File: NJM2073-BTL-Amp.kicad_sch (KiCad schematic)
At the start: 84 parts, among them J1 Screw_Terminal_01x02, J2 Screw_Terminal_01x02, J3 Barrel_Jack_Switch, J4 Conn_Coaxial_x2, J5 AudioJack3_SwitchTR, U1 NJM2073, U2 NJM2073, U3 NJM4558, U4 NJM4558, U5 LM317_TO-220

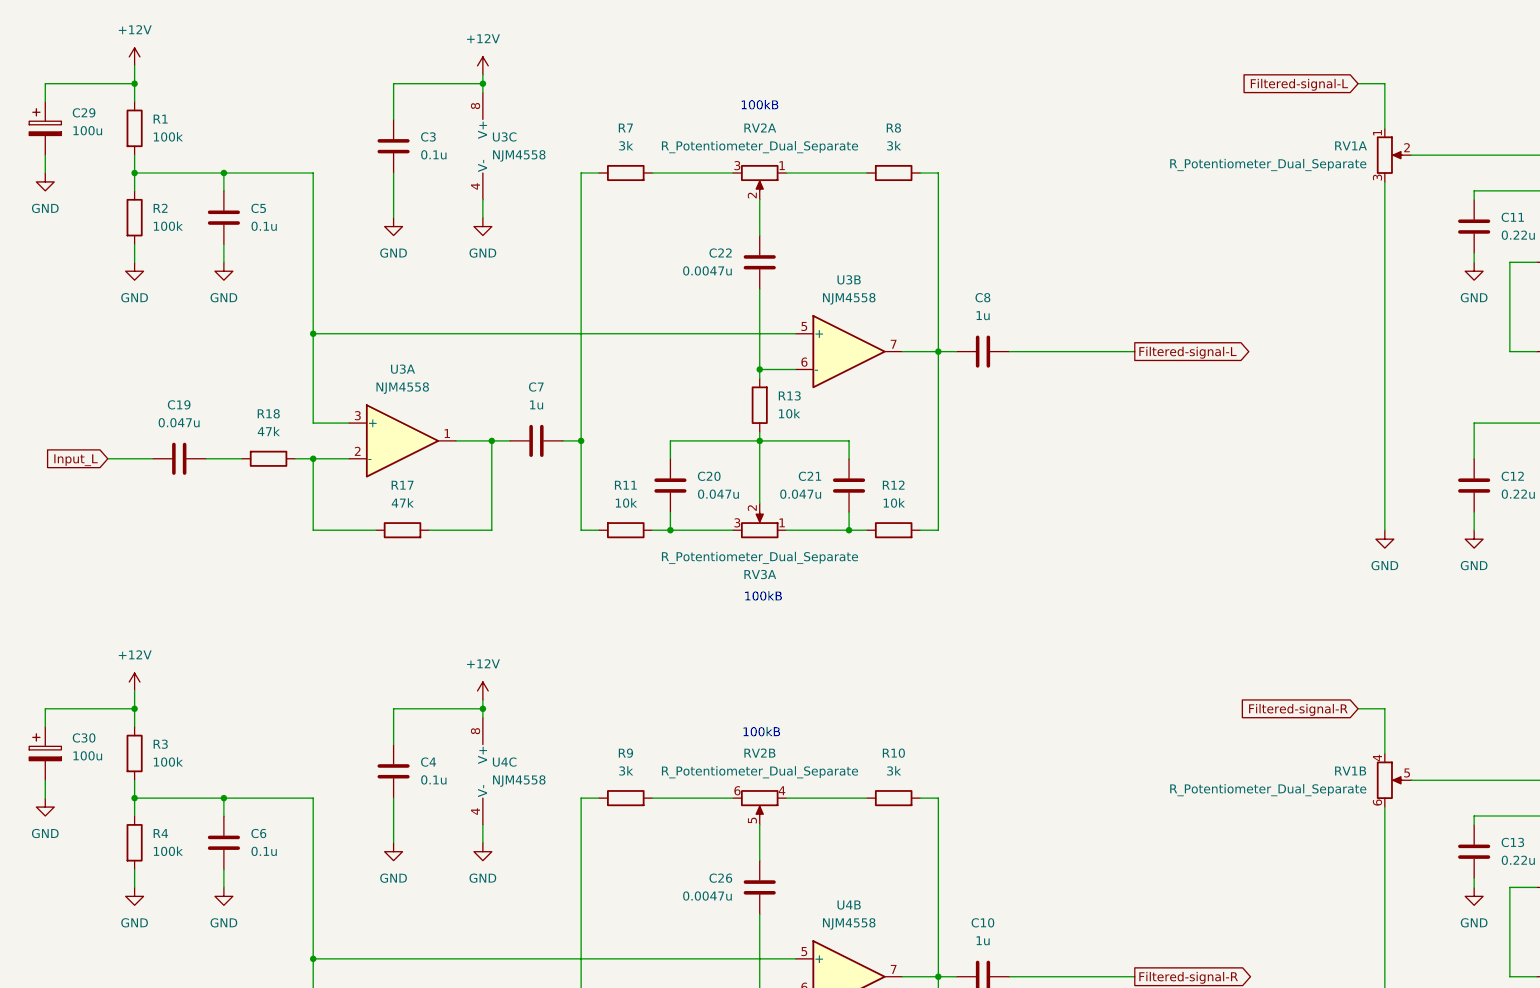
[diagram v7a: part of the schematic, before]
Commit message: 配線修正
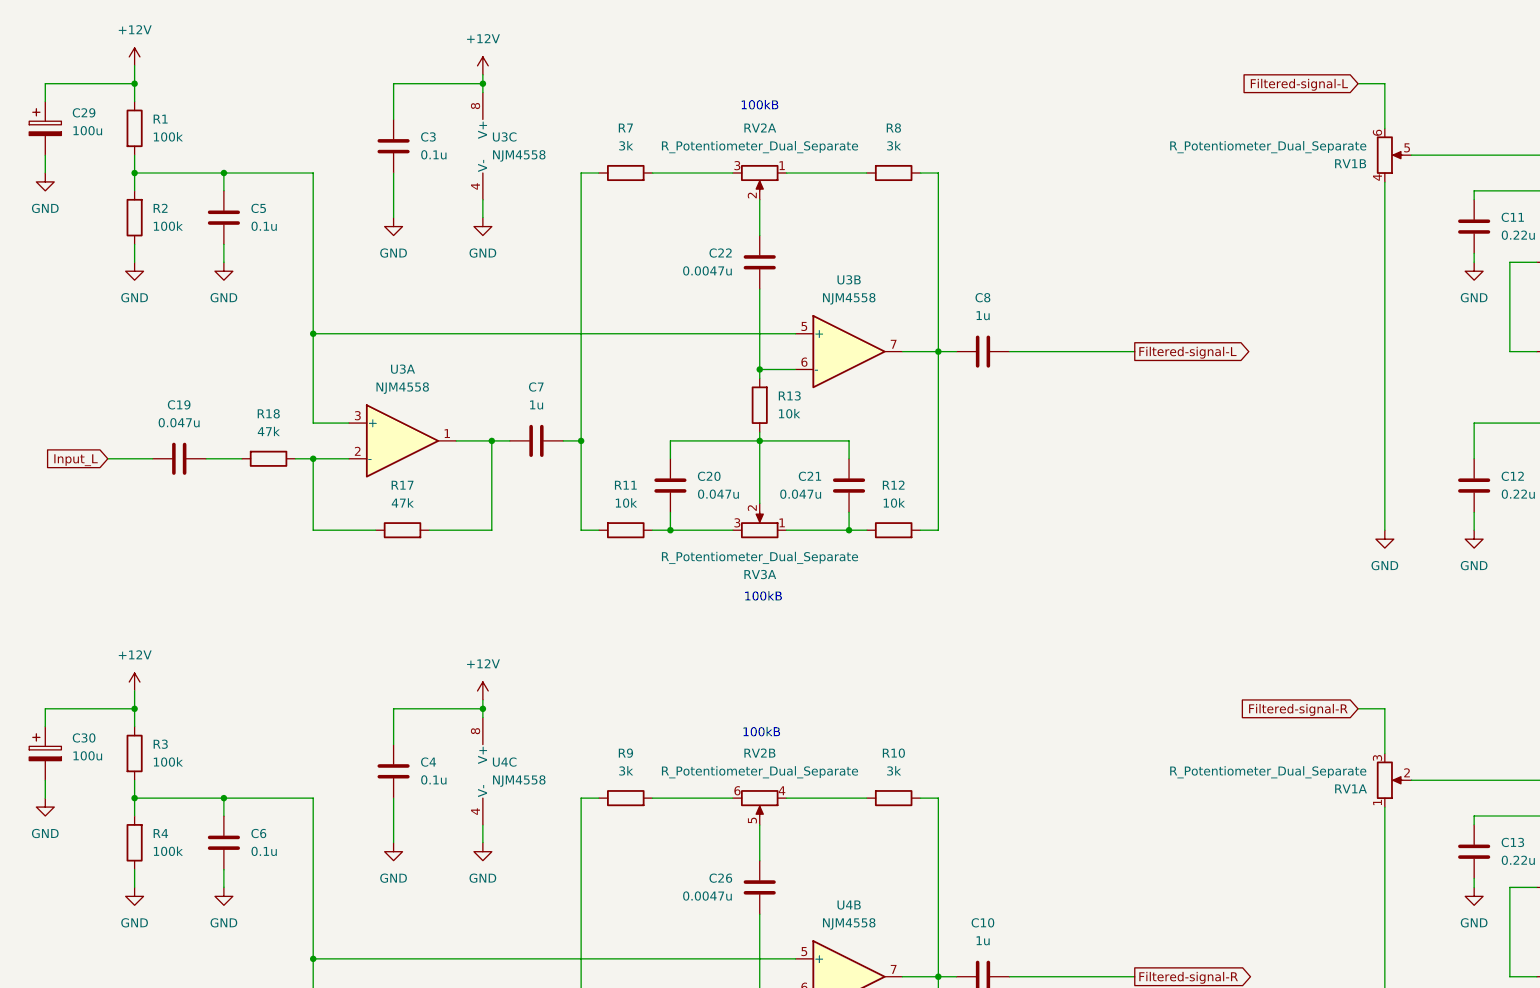
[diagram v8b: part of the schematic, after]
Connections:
- net Filtered-signal-L: now also RV1.6; no longer RV1.1
- net Filtered-signal-R: now also RV1.3; no longer RV1.4
- net GND: now also R2.1, R4.1, RV1.1, RV1.4; no longer R2.2, R4.2, RV1.3, RV1.6
- net at U2.7 (AIN+): now also RV1.2; no longer RV1.5
- net at C6.1, R3.2, U4.3 (+)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: now also R4.2; no longer R4.1
- net at C10.1, R15.2, U4.7: now also R10.1; no longer R10.2
- net at C5.1, R1.2, U3.3 (+)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: now also R2.2; no longer R2.1
- net at U1.7 (AIN+): now also RV1.5; no longer RV1.2
- net at RV2.4: now also R10.2; no longer R10.1
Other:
- moved on the sheet: R10, R2, R4
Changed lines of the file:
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@@
 	)
 	(symbol
+		(lib_id "Device:R_Potentiometer_Dual_Separate")
+		(at 292.1 137.16 0)
+		(mirror x)
+		(unit 1)
+		(exclude_from_sim no)
+		(in_bom yes)
+		(on_board yes)
+		(dnp no)
+		(property "Reference" "RV1"
+			(at 289.56 138.4301 0)
+			(effects
+				(font
+					(size 1.27 1.27)
+				)
+				(justify right)
+			)
+		)
+		(property "Value" "R_Potentiometer_Dual_Separate"
+			(at 289.56 135.8901 0)
+			(effects
+				(font
+					(size 1.27 1.27)
+				)
+				(justify right)
+			)
+		)
+		(property "Footprint" "Potentiometer_THT:Potentiometer_Alps_RK097_Dual_Horizontal"
+			(at 292.1 137.16 0)
+			(effects
+				(font
+					(size 1.27 1.27)
+				)
+				(hide yes)
+			)
+		)
+		(property "Datasheet" "~"
+			(at 292.1 137.16 0)
+			(effects
+				(font
+					(size 1.27 1.27)
+				)
+				(hide yes)
+			)
+		)
+		(property "Description" "Dual potentiometer, separate units"
+			(at 292.1 137.16 0)
+			(effects
+				(font
+					(size 1.27 1.27)
+				)
+				(hide yes)
+			)
+		)
+		(pin "2"
+		)
+		(pin "5"
+		)
+		(pin "1"
+		)
+		(pin "3"
+		)
+		(pin "4"
+		)
+		(pin "6"
+		)
+		(instances
+			(project "NJM2073-BTL-Amp"
+				(path "/39400954-8ff9-4acb-a709-09671291994b"
+					(reference "RV1")
+					(unit 1)
+				)
+			)
+		)
+	)
+	(symbol
 		(lib_id "power:GND")
 		(at 323.85 101.6 0)
@@
 	(symbol
 		(lib_id "Device:R")
-		(at 114.3 57.15 0)
+		(at 114.3 57.15 180)
 		(unit 1)
 		(exclude_from_sim no)
@@
 					(size 1.27 1.27)
 				)
-				(justify left)
+				(justify right)
 			)
 		)
@@
 					(size 1.27 1.27)
 				)
-				(justify left)
+				(justify right)
 			)
 		)
 		(property "Footprint" "Resistor_THT:R_Axial_DIN0207_L6.3mm_D2.5mm_P10.16mm_Horizontal"
-			(at 112.522 57.15 90)
+			(at 116.078 57.15 90)
 			(effects
 				(font
@@
 	)
 	(symbol
-		(lib_id "Device:R_Potentiometer_Dual_Separate")
-		(at 292.1 137.16 0)
-		(unit 2)
-		(exclude_from_sim no)
-		(in_bom yes)
-		(on_board yes)
-		(dnp no)
-		(fields_autoplaced yes)
-		(property "Reference" "RV1"
-			(at 289.56 135.8899 0)
-			(effects
-				(font
-					(size 1.27 1.27)
-				)
-				(justify right)
-			)
-		)
-		(property "Value" "R_Potentiometer_Dual_Separate"
-			(at 289.56 138.4299 0)
-			(effects
-				(font
-					(size 1.27 1.27)
-				)
-				(justify right)
-			)
-		)
-		(property "Footprint" "Potentiometer_THT:Potentiometer_Alps_RK097_Dual_Horizontal"
-			(at 292.1 137.16 0)
-			(effects
-				(font
-					(size 1.27 1.27)
-				)
-				(hide yes)
-			)
-		)
-		(property "Datasheet" "~"
-			(at 292.1 137.16 0)
-			(effects
-				(font
-					(size 1.27 1.27)
-				)
-				(hide yes)
-			)
-		)
-		(property "Description" "Dual potentiometer, separate units"
-			(at 292.1 137.16 0)
-			(effects
-				(font
-					(size 1.27 1.27)
-				)
-				(hide yes)
-			)
-		)
-		(pin "2"
-		)
-		(pin "5"
-		)
-		(pin "1"
-		)
-		(pin "3"
-		)
-		(pin "4"
-		)
-		(pin "6"
-		)
-		(instances
-			(project ""
-				(path "/39400954-8ff9-4acb-a709-09671291994b"
-					(reference "RV1")
-					(unit 2)
-				)
-			)
-		)
-	)
-	(symbol
 		(lib_id "power:GND")
 		(at 163.83 57.15 0)
@@
 	)
 	(symbol
+		(lib_id "Device:R_Potentiometer_Dual_Separate")
+		(at 292.1 48.26 0)
+		(mirror x)
+		(unit 2)
+		(exclude_from_sim no)
+		(in_bom yes)
+		(on_board yes)
+		(dnp no)
+		(property "Reference" "RV1"
+			(at 289.56 49.5301 0)
+			(effects
+				(font
+					(size 1.27 1.27)
+				)
+				(justify right)
+			)
+		)
+		(property "Value" "R_Potentiometer_Dual_Separate"
+			(at 289.56 46.9901 0)
+			(effects
+				(font
+					(size 1.27 1.27)
+				)
+				(justify right)
+			)
+		)
+		(property "Footprint" "Potentiometer_THT:Potentiometer_Alps_RK097_Dual_Horizontal"
+			(at 292.1 48.26 0)
+			(effects
+				(font
+					(size 1.27 1.27)
+				)
+				(hide yes)
+			)
+		)
+		(property "Datasheet" "~"
+			(at 292.1 48.26 0)
+			(effects
+				(font
+					(size 1.27 1.27)
+				)
+				(hide yes)
+			)
+		)
+		(property "Description" "Dual potentiometer, separate units"
+			(at 292.1 48.26 0)
+			(effects
+				(font
+					(size 1.27 1.27)
+				)
+				(hide yes)
+			)
+		)
+		(pin "2"
+		)
+		(pin "5"
+		)
+		(pin "1"
+		)
+		(pin "3"
+		)
+		(pin "4"
+		)
+		(pin "6"
+		)
+		(instances
+			(project "NJM2073-BTL-Amp"
+				(path "/39400954-8ff9-4acb-a709-09671291994b"
+					(reference "RV1")
+					(unit 2)
+				)
+			)
+		)
+	)
+	(symbol
 		(lib_id "Device:R")
-		(at 222.25 139.7 90)
+		(at 222.25 139.7 270)
 		(unit 1)
 		(exclude_from_sim no)
@@
 		)
 		(property "Footprint" "Resistor_THT:R_Axial_DIN0207_L6.3mm_D2.5mm_P10.16mm_Horizontal"
-			(at 222.25 141.478 90)
+			(at 222.25 137.922 90)
 			(effects
 				(font
@@
 	)
 	(symbol
-		(lib_id "Device:R_Potentiometer_Dual_Separate")
-		(at 292.1 48.26 0)
-		(unit 1)
-		(exclude_from_sim no)
-		(in_bom yes)
-		(on_board yes)
-		(dnp no)
-		(fields_autoplaced yes)
-		(property "Reference" "RV1"
-			(at 289.56 46.9899 0)
-			(effects
-				(font
-					(size 1.27 1.27)
-				)
-				(justify right)
-			)
-		)
-		(property "Value" "R_Potentiometer_Dual_Separate"
-			(at 289.56 49.5299 0)
-			(effects
-				(font
-					(size 1.27 1.27)
-				)
-				(justify right)
-			)
-		)
-		(property "Footprint" "Potentiometer_THT:Potentiometer_Alps_RK097_Dual_Horizontal"
-			(at 292.1 48.26 0)
-			(effects
-				(font
-					(size 1.27 1.27)
-				)
-				(hide yes)
-			)
-		)
-		(property "Datasheet" "~"
-			(at 292.1 48.26 0)
-			(effects
-				(font
-					(size 1.27 1.27)
-				)
-				(hide yes)
-			)
-		)
-		(property "Description" "Dual potentiometer, separate units"
-			(at 292.1 48.26 0)
-			(effects
-				(font
-					(size 1.27 1.27)
-				)
-				(hide yes)
-			)
-		)
-		(pin "2"
-		)
-		(pin "5"
-		)
-		(pin "1"
-		)
-		(pin "3"
-		)
-		(pin "4"
-		)
-		(pin "6"
-		)
-		(instances
-			(project ""
-				(path "/39400954-8ff9-4acb-a709-09671291994b"
-					(reference "RV1")
-					(unit 1)
-				)
-			)
-		)
-	)
-	(symbol
 		(lib_id "Device:L")
 		(at 57.15 25.4 90)
@@
 	(symbol
 		(lib_id "Device:R")
-		(at 114.3 146.05 0)
+		(at 114.3 146.05 180)
 		(unit 1)
 		(exclude_from_sim no)
@@
 					(size 1.27 1.27)
 				)
-				(justify left)
+				(justify right)
 			)
 		)
@@
 					(size 1.27 1.27)
 				)
-				(justify left)
+				(justify right)
 			)
 		)
 		(property "Footprint" "Resistor_THT:R_Axial_DIN0207_L6.3mm_D2.5mm_P10.16mm_Horizontal"
-			(at 112.522 146.05 90)
+			(at 116.078 146.05 90)
 			(effects
 				(font
